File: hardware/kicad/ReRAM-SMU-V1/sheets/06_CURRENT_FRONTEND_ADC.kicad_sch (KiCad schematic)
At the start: 21 parts, among them U11 ADA4522-2 CH1 P-leg zero-drif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, U12 ADA4522-2 CH2 N-leg (unity, r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, U13 OPA140 P-leg JFET 0.5pA *HIGH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, U14 OPA140 N-leg JFET <1pA unity, U31 ADS1262 (supply corrected: co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

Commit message: hardware: pre-ERC correction gate 3 (ADS1262 Table 6-1, AD5764 32-pin C-grade, buffer 1000x fix, BAV199 after buffer, LT5400 EP floating, pin audit pass)
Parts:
- D1: value BAV199 low-leak 3pA clamp to AVDD -> BAV199 3pA typical (max nA at VR=75V, not guaranteed) — PRIMARY 1uA/100nA clamp AFTER OPA140 buffer, pre-buffer BAV199 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
- D2: value BAV199 clamp to AVSS/GND -> BAV199 3pA typical (max nA at VR=75V, not guaranteed) — PRIMARY 1uA/100nA clamp AFTER OPA140 buffer, pre-buffer BAV199 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
- D3: value BAV199 N-leg to AVDD -> BAV199 3pA typical (max nA at VR=75V, not guaranteed) — PRIMARY 1uA/100nA clamp AFTER OPA140 buffer, pre-buffer BAV199 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
- D4: value BAV199 N-leg to AVSS -> BAV199 3pA typical (max nA at VR=75V, not guaranteed) — PRIMARY 1uA/100nA clamp AFTER OPA140 buffer, pre-buffer BAV199 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
- R11: value 1.00k 0.1% 25ppm PROT_P (≤5pA leak w/ BAV199) -> 1.00k 0.1% 25ppm PROT_P (≤5pA leak w/ BAV199 3pA typical (max nA at VR=75V, not guaranteed) — PRIMARY 1uA/100nA clamp A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
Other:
- note added: "ADS1262 allocation: AIN0=SHUNT_P, AIN1=SHUNT_N (diff), AIN2=REFP LTC6655-2.5, AIN3=REFN GND — ref via AIN multifunction, no REFP/REFN pins"
- note added: "Chain: ISENSE_P/N_K → R_prot 1k + BAV199 3pA typical (max nA at VR=75V, not guaranteed) — PRIMARY 1uA/100nA clamp AFTER OPA140 buffer, pre-buffer BAV199 DNP/prototype (leakage must not load shunt)(3pA) clamp (NO TVS) → RC 1k+10n C0G (8kHz diff) → Buffer → VCM=2.5V shift → 1k+1n → AIN0/1 (PGAL/H monitor)"
- note added: "LAYOUT: BAV199 3pA typical (max nA at VR=75V, not guaranteed) — PRIMARY 1uA/100nA clamp AFTER OPA140 buffer, pre-buffer BAV199 DNP/prototype (leakage must not load shunt) + RC + buffers adjacent, guard keepout on OPA140 inputs (exposed ring, 0.5mm gap, stitched inner plane DNP, local 100n). R_prot before clamp, RC after."
- note added: "Mandatory: CAPP(4)-CAPN(5) 4.7nF C0G, REFOUT(8) 1uF+0.1uF to AVSS, BYPASS(17) 1uF to AVSS, XTAL1(15) internal: tie to DGND, XTAL2(16) NC (or crystal 7.3728MHz)"
- note added: "REF: LTC6655-2.5 LN REFP/REFN 10u+100n. AVDD 5V AVSS 0V (0.3 cushion) DVDD 3V3. AINCOM=2.5V from divider. DRDY/status PGAL/H flag checked. No TVS on high-Z — BAV199 3pA typical (max nA at VR=75V, not guaranteed) — PRIMARY 1uA/100nA clamp AFTER OPA140 buffer, pre-buffer BAV199 DNP/prototype (leakage must not load shunt) only."
- note removed: "Chain: ISENSE_P/N_K → R_prot 1k + BAV199(3pA) clamp (NO TVS) → RC 1k+10n C0G (8kHz diff) → Buffer → VCM=2.5V shift → 1k+1n → AIN0/1 (PGAL/H monitor)"
- note removed: "LAYOUT: BAV199 + RC + buffers adjacent, guard keepout on OPA140 inputs (exposed ring, 0.5mm gap, stitched inner plane DNP, local 100n). R_prot before clamp, RC after."
- note removed: "REF: LTC6655-2.5 LN REFP/REFN 10u+100n. AVDD 5V AVSS 0V (0.3 cushion) DVDD 3V3. AINCOM=2.5V from divider. DRDY/status PGAL/H flag checked. No TVS on high-Z — BAV199 only."
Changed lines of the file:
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@@
 	(global_label "ADC_SPI_MISO" (shape bidirectional) (at 150 30 0) (fields_autoplaced yes) (uuid "spi-miso"))
 	(global_label "ADC_SPI_CS" (shape bidirectional) (at 150 35 0) (fields_autoplaced yes) (uuid "spi-cs"))
-	; --- Protection R 1k + diodes BAV199 per leg (no TVS) ---
+	; --- Protection R 1k + diodes BAV199 3pA typical (max nA at VR=75V, not guaranteed) — PRIMARY 1uA/100nA clamp AFTER OPA140 buffer, pre-buffer BAV199 DNP/prototype (leakage must not load shunt) per leg (no TVS) ---
 	(symbol (lib_id "Device:R") (at 30 25 0) (unit 1) (exclude_from_sim no) (in_bom yes) (on_board yes) (dnp no)
 		(uuid "rprot-p") (property "Reference" "R11" (at 30 28.5 0) (effects (font (size 1.0 1.0))))
-		(property "Value" "1.00k 0.1% 25ppm PROT_P (≤5pA leak w/ BAV199)" (at 30 21 0) (effects (font (size 1.0 1.0))))
+		(property "Value" "1.00k 0.1% 25ppm PROT_P (≤5pA leak w/ BAV199 3pA typical (max nA at VR=75V, not guaranteed) — PRIMARY 1uA/100nA clamp AFTER OPA140 buffer, pre-buffer BAV199 DNP/prototype (leakage must not load shunt))" (at 30 21 0) (effects (font (size 1.0 1.0))))
 		(property "Footprint" "Resistor_SMD:R_0805_2012Metric" (at 30 19.5 0) (effects (font (size 1.0 1.0)) (hide yes)))
 		(pin "1" (uuid "r11-1")) (pin "2" (uuid "r11-2"))
@@
 	(symbol (lib_id "Device:D") (at 50 20 0) (unit 1) (exclude_from_sim no) (in_bom yes) (on_board yes) (dnp no)
 		(uuid "d1-uuid") (property "Reference" "D1" (at 50 23.5 0) (effects (font (size 1.0 1.0))))
-		(property "Value" "BAV199 low-leak 3pA clamp to AVDD" (at 50 16 0) (effects (font (size 1.0 1.0))))
+		(property "Value" "BAV199 3pA typical (max nA at VR=75V, not guaranteed) — PRIMARY 1uA/100nA clamp AFTER OPA140 buffer, pre-buffer BAV199 DNP/prototype (leakage must not load shunt) low-leak 3pA clamp to AVDD" (at 50 16 0) (effects (font (size 1.0 1.0))))
 		(property "Footprint" "Diode_SMD:D_SOT-23" (at 50 14.5 0) (effects (font (size 1.0 1.0)) (hide yes)))
 		(pin "1") (pin "2")
@@
 	(symbol (lib_id "Device:D") (at 50 40 0) (unit 1) (exclude_from_sim no) (in_bom yes) (on_board yes) (dnp no)
 		(uuid "d2-uuid") (property "Reference" "D2" (at 50 43.5 0) (effects (font (size 1.0 1.0))))
-		(property "Value" "BAV199 clamp to AVSS/GND" (at 50 46 0) (effects (font (size 1.0 1.0))))
+		(property "Value" "BAV199 3pA typical (max nA at VR=75V, not guaranteed) — PRIMARY 1uA/100nA clamp AFTER OPA140 buffer, pre-buffer BAV199 DNP/prototype (leakage must not load shunt) clamp to AVSS/GND" (at 50 46 0) (effects (font (size 1.0 1.0))))
 		(pin "1") (pin "2")
 	)
 	(symbol (lib_id "Device:D") (at 50 30 180) (unit 1) (exclude_from_sim no) (in_bom yes) (on_board yes) (dnp no)
 		(uuid "d3-uuid") (property "Reference" "D3" (at 50 33.5 0) (effects (font (size 1.0 1.0))))
-		(property "Value" "BAV199 N-leg to AVDD" (at 50 30 0) (effects (font (size 1.0 1.0)) (hide yes)))
+		(property "Value" "BAV199 3pA typical (max nA at VR=75V, not guaranteed) — PRIMARY 1uA/100nA clamp AFTER OPA140 buffer, pre-buffer BAV199 DNP/prototype (leakage must not load shunt) N-leg to AVDD" (at 50 30 0) (effects (font (size 1.0 1.0)) (hide yes)))
 		(pin "1") (pin "2")
 	)
 	(symbol (lib_id "Device:D") (at 50 50 180) (unit 1) (exclude_from_sim no) (in_bom yes) (on_board yes) (dnp no)
 		(uuid "d4-uuid") (property "Reference" "D4" (at 50 53.5 0) (effects (font (size 1.0 1.0))))
-		(property "Value" "BAV199 N-leg to AVSS" (at 50 46 0) (effects (font (size 1.0 1.0)) (hide yes)))
+		(property "Value" "BAV199 3pA typical (max nA at VR=75V, not guaranteed) — PRIMARY 1uA/100nA clamp AFTER OPA140 buffer, pre-buffer BAV199 DNP/prototype (leakage must not load shunt) N-leg to AVSS" (at 50 46 0) (effects (font (size 1.0 1.0)) (hide yes)))
 		(pin "1") (pin "2")
 	)
@@
 	(global_label "AVSS_-2V5" (shape input) (at 125.0 50.0 0) (uuid "avss25-glob") (property "Intersheetrefs" "${INTERSHEET_REFS}"))
 	(text "Bipolar ±2.5V PRIMARY physically (AVDD +2.5V LT3045 / AVSS -2.5V LT1964) — DEC-042 supersedes DEC-034 VCM" (at 10 100 0) (effects (font (size 1 1)) (justify left)))
+	(text "ADS1262 allocation: AIN0=SHUNT_P, AIN1=SHUNT_N (diff), AIN2=REFP LTC6655-2.5, AIN3=REFN GND — ref via AIN multifunction, no REFP/REFN pins" (at 10 95 0) (effects (font (size 0.9 0.9)) (justify left)))
+	(text "Mandatory: CAPP(4)-CAPN(5) 4.7nF C0G, REFOUT(8) 1uF+0.1uF to AVSS, BYPASS(17) 1uF to AVSS, XTAL1(15) internal: tie to DGND, XTAL2(16) NC (or crystal 7.3728MHz)" (at 10 100 0) (effects (font (size 0.9 0.9)) (justify left)))
 (wire (pts (xy 10 25) (xy 28 25)) (stroke (width 0.254) (type default)) (uuid "w-p-kelvin"))
 	(wire (pts (xy 10 35) (xy 28 35)) (stroke (width 0.254) (type default)) (uuid "w-n-kelvin"))
@@
 	(wire (pts (xy 128 45) (xy 129 42)) (stroke (width 0.15) (type default)) (uuid "w-adc-ainn"))
 	(text "06_CURRENT_FRONTEND_ADC — Gate F detailed: ADS1262 (supply corrected: compare +2.5V VCM vs ±2.5V bipolar direct GND-centered; PREFER bipolar ±2.5V for 100nA low-leakage, see DEC-039)IPW TSSOP-28 PW (was TQFP-28, SBAS661C) re-derived (VREF 2.5, PGA 1-32, FSR=±VREF/G, AIN 0.3..4.7V, PGAL_ALM)" (at 10 5 0) (effects (font (size 1.0 1.0)) (justify left)))
-	(text "Chain: ISENSE_P/N_K → R_prot 1k + BAV199(3pA) clamp (NO TVS) → RC 1k+10n C0G (8kHz diff) → Buffer → VCM=2.5V shift → 1k+1n → AIN0/1 (PGAL/H monitor)" (at 10 8 0) (effects (font (size 0.9 0.9)) (justify left)))
+	(text "Chain: ISENSE_P/N_K → R_prot 1k + BAV199 3pA typical (max nA at VR=75V, not guaranteed) — PRIMARY 1uA/100nA clamp AFTER OPA140 buffer, pre-buffer BAV199 DNP/prototype (leakage must not load shunt)(3pA) clamp (NO TVS) → RC 1k+10n C0G (8kHz diff) → Buffer → VCM=2.5V shift → 1k+1n → AIN0/1 (PGAL/H monitor)" (at 10 8 0) (effects (font (size 0.9 0.9)) (justify left)))
 	(text "Buffers: ADA4522 (<5uV, 50pA) for 2.5R-5k (10mA-10uA) + OPA140 (0.5pA typ, 10pA max JFET) for 100k/1M (1uA/100nA) — <10pA audit 7.5pA typ" (at 10 80 0) (effects (font (size 0.9 0.9)) (justify left)))
 	(text "PGA table: 10mA/1mA 25mV→PGA32 FS78mV 32% (preGain 3.13 DNP) | 100uA/10uA 50mV→PGA32 64% (1.56 DNP) | 1uA/100nA 100mV→PGA16 FS156 64% (*PGA32 clips*)" (at 10 83 0) (effects (font (size 0.9 0.9)) (justify left)))
 	(text "External gain: NOT mandatory — PGA covers FS with 1.56-3.13x headroom. Hybrid amp needed for LEVEL SHIFT (0V→2.5V VCM) + leakage isolation (ADC 2nA bias cannot drive 1M)" (at 10 86 0) (effects (font (size 0.9 0.9)) (justify left)))
-	(text "REF: LTC6655-2.5 LN REFP/REFN 10u+100n. AVDD 5V AVSS 0V (0.3 cushion) DVDD 3V3. AINCOM=2.5V from divider. DRDY/status PGAL/H flag checked. No TVS on high-Z — BAV199 only." (at 10 89 0) (effects (font (size 0.9 0.9)) (justify left)))
-	(text "LAYOUT: BAV199 + RC + buffers adjacent, guard keepout on OPA140 inputs (exposed ring, 0.5mm gap, stitched inner plane DNP, local 100n). R_prot before clamp, RC after." (at 10 92 0) (effects (font (size 0.9 0.9)) (justify left)))
+	(text "REF: LTC6655-2.5 LN REFP/REFN 10u+100n. AVDD 5V AVSS 0V (0.3 cushion) DVDD 3V3. AINCOM=2.5V from divider. DRDY/status PGAL/H flag checked. No TVS on high-Z — BAV199 3pA typical (max nA at VR=75V, not guaranteed) — PRIMARY 1uA/100nA clamp AFTER OPA140 buffer, pre-buffer BAV199 DNP/prototype (leakage must not load shunt) only." (at 10 89 0) (effects (font (size 0.9 0.9)) (justify left)))
+	(text "LAYOUT: BAV199 3pA typical (max nA at VR=75V, not guaranteed) — PRIMARY 1uA/100nA clamp AFTER OPA140 buffer, pre-buffer BAV199 DNP/prototype (leakage must not load shunt) + RC + buffers adjacent, guard keepout on OPA140 inputs (exposed ring, 0.5mm gap, stitched inner plane DNP, local 100n). R_prot before clamp, RC after." (at 10 92 0) (effects (font (size 0.9 0.9)) (justify left)))
 	(text "RE-DERIVED per TI SBAS661C Eq12/Table7-1: |FSR|=VREF/G, 0.3<=AIN<=4.7, VCM=2.5 +/- G*Vdiff/2 <0.3/4.7 — compliant for all 6 shunts. See docs/calculations/ADS1262 (supply corrected: compare +2.5V VCM vs ±2.5V bipolar direct GND-centered; PREFER bipolar ±2.5V for 100nA low-leakage, see DEC-039)IPW TSSOP-28 PW (was TQFP-28, SBAS661C)_ANALOG_RANGE_DERIVATION.md" (at 10 95 0) (effects (font (size 0.9 0.9)) (justify left)))
 	(sheet_instances

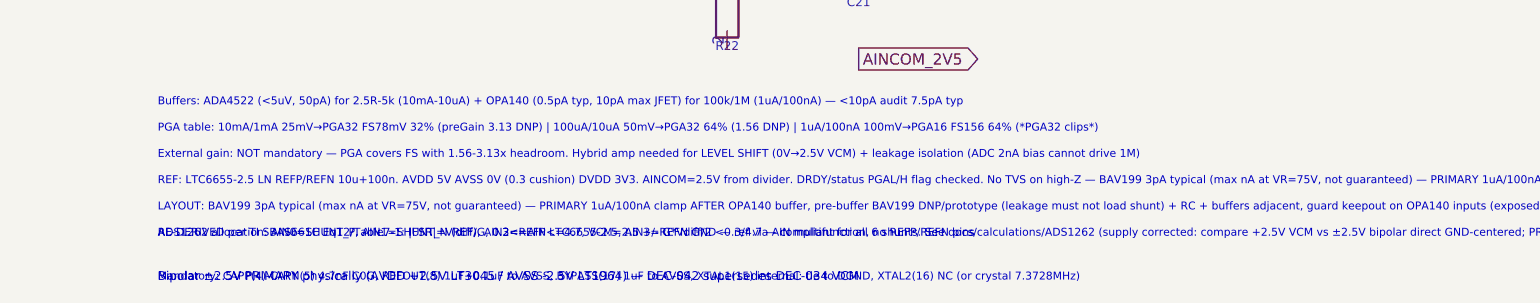
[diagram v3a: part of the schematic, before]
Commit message: hardware: preflight fix ADS1262 BYPASS->DGND, pin types, LT5400 EP floating doc + pin_audit tool
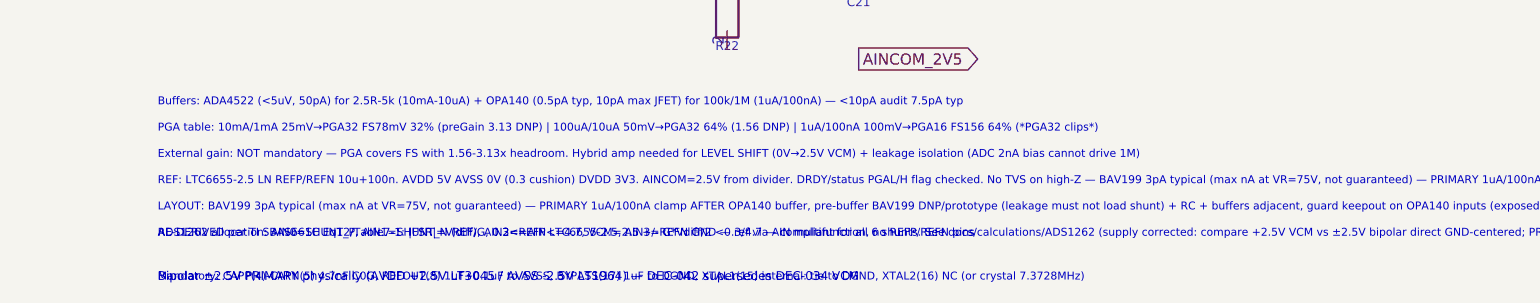
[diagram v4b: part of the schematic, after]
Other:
- note added: "Mandatory: CAPP(4)-CAPN(5) 4.7nF C0G, REFOUT(8) 1uF+0.1uF to AVSS, BYPASS(17) 1uF to DGND, XTAL1(15) internal: tie to DGND, XTAL2(16) NC (or crystal 7.3728MHz)"
- note removed: "Mandatory: CAPP(4)-CAPN(5) 4.7nF C0G, REFOUT(8) 1uF+0.1uF to AVSS, BYPASS(17) 1uF to AVSS, XTAL1(15) internal: tie to DGND, XTAL2(16) NC (or crystal 7.3728MHz)"
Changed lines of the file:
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@@
 	(text "Bipolar ±2.5V PRIMARY physically (AVDD +2.5V LT3045 / AVSS -2.5V LT1964) — DEC-042 supersedes DEC-034 VCM" (at 10 100 0) (effects (font (size 1 1)) (justify left)))
 	(text "ADS1262 allocation: AIN0=SHUNT_P, AIN1=SHUNT_N (diff), AIN2=REFP LTC6655-2.5, AIN3=REFN GND — ref via AIN multifunction, no REFP/REFN pins" (at 10 95 0) (effects (font (size 0.9 0.9)) (justify left)))
-	(text "Mandatory: CAPP(4)-CAPN(5) 4.7nF C0G, REFOUT(8) 1uF+0.1uF to AVSS, BYPASS(17) 1uF to AVSS, XTAL1(15) internal: tie to DGND, XTAL2(16) NC (or crystal 7.3728MHz)" (at 10 100 0) (effects (font (size 0.9 0.9)) (justify left)))
+	(text "Mandatory: CAPP(4)-CAPN(5) 4.7nF C0G, REFOUT(8) 1uF+0.1uF to AVSS, BYPASS(17) 1uF to DGND, XTAL1(15) internal: tie to DGND, XTAL2(16) NC (or crystal 7.3728MHz)" (at 10 100 0) (effects (font (size 0.9 0.9)) (justify left)))
 (wire (pts (xy 10 25) (xy 28 25)) (stroke (width 0.254) (type default)) (uuid "w-p-kelvin"))
 	(wire (pts (xy 10 35) (xy 28 35)) (stroke (width 0.254) (type default)) (uuid "w-n-kelvin"))

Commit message: Beta
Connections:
- net ADC_AINN: now also C41.1, C41.2, U31.18 (DGND)
- net ADC_AINP: now also U31.19 (DVDD), U31.23 (AIN2)
- net ADC_DRDY: now also U31.4 (CAPP)
- net ADC_SPI_CS: now also U31.20 (RESET/PWDN), U31.22 (AIN1), U31.25 (AIN4), U31.8 (REFOUT)
- net ADC_SPI_MISO: now also U31.5 (CAPN)
- net ADC_SPI_MOSI: now also U31.21 (AIN0), U31.6 (AVDD)
- net ADC_SPI_SCLK: now also U31.7 (AVSS)
- net AINCOM_2V5: now also C13.1, C13.2, C21.1, C21.2, R21.1, R21.2, R22.1, R22.2
- net AVDD_+2V5: now also C31.1, C31.2, R31.1, R31.2, U31.12 (DIN)
- net AVSS_-2V5: now also R32.1, R32.2, U31.10 (CS), U31.11 (SCLK), U31.13 (DOUT/DRDY), U31.14 (DRDY), U31.9 (START)
- net ISENSE_N_K: now also C11.2, R12.1, R12.2
- net ISENSE_P_K: now also C11.1, C12.2, R11.1, R11.2
- net VREF_2V5: now also C12.1
- no-connect marks 0 -> 8
